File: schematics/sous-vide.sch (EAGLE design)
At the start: 32 parts, among them IC1 MEGA8-P, T1 BC547, T2 BC547, T3 BC547

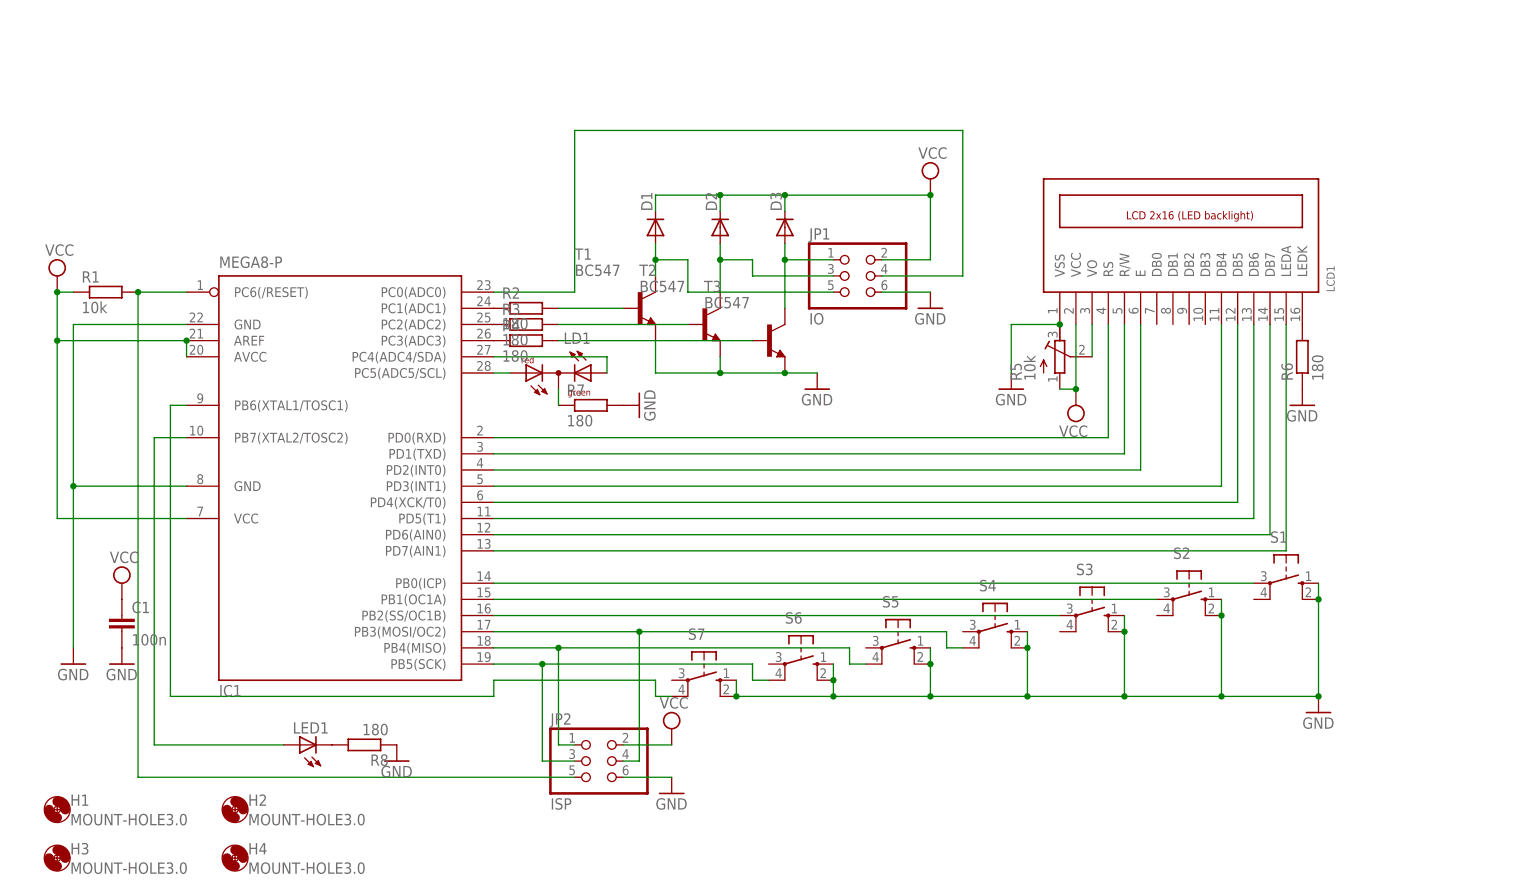
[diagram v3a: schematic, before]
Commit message: Removed button and LED and added crystal for more precise timing over longer periods.
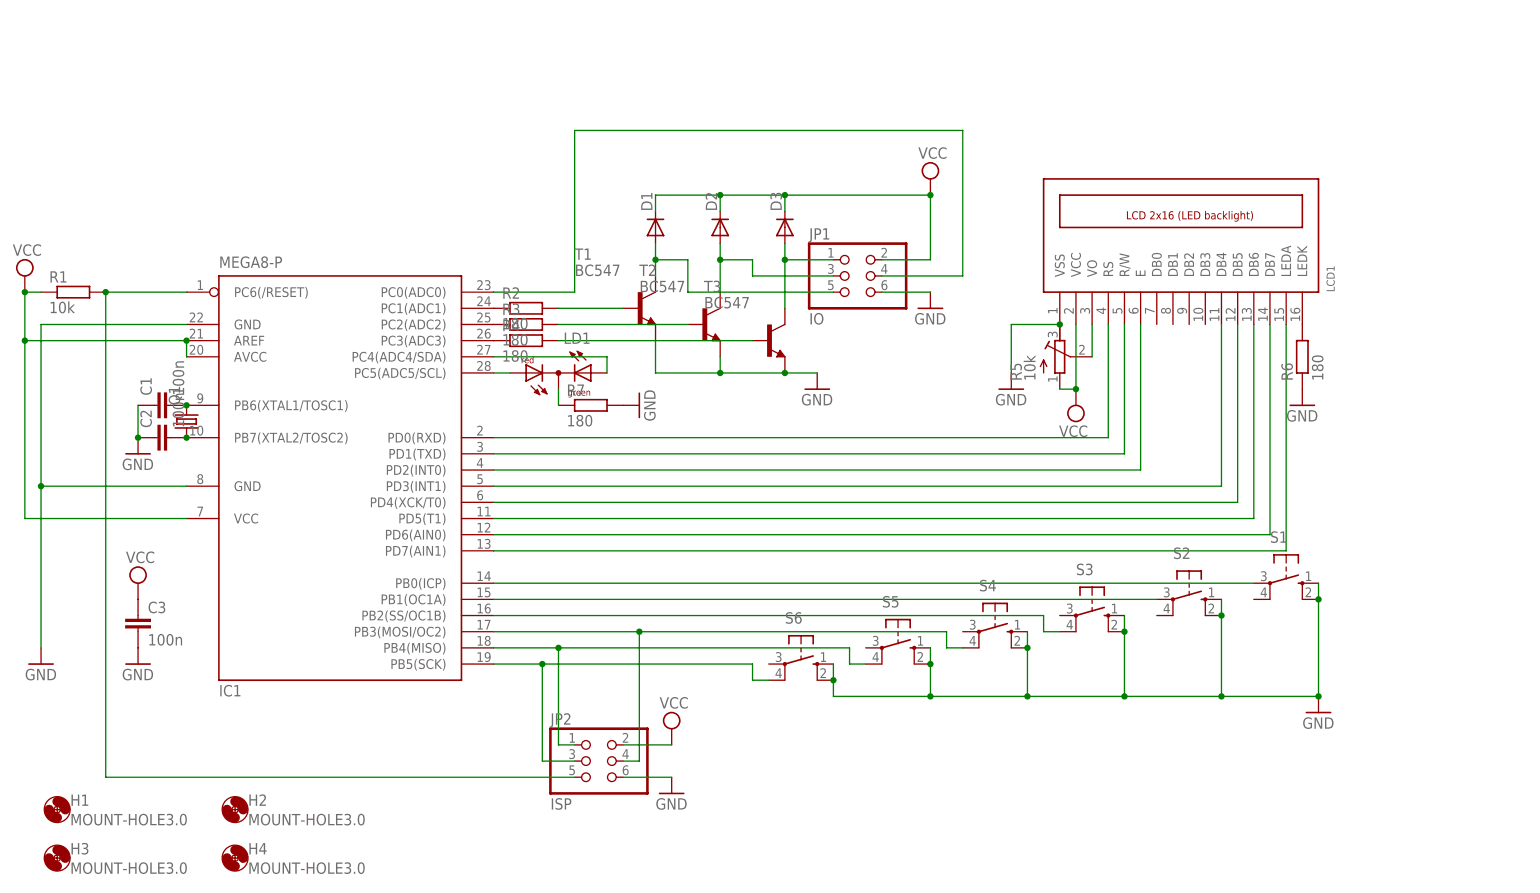
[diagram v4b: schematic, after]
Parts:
- removed LED1: (no value), led:LED3MM
- removed R8: 180, rcl:R-EU_0207/2V
- removed S7: (no value), switch-omron:40-XX
- added C2, C3: 100n, resistor:C-EU025-025X050
- added Q1: (no value), crystal:CRYSTALHC49U-V
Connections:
- removed net N$26: IC1.PB6(XTAL1/TOSC1), S7.P1
- net GND: now also C1.1, C2.1, C3.2; no longer C1.2, R8.1, S7.S, S7.S1
- net N$1: now also C1.2, IC1.PB6(XTAL1/TOSC1), Q1.2; no longer LED1.C, R8.2
- net N$15: now also C2.2, Q1.1; no longer LED1.A
- net N$35: now also S3.P1; no longer S3.P
- net VCC: now also C3.1; no longer C1.1
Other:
- moved on the sheet: C1, R1

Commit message: PCB button and connector layout rearranged. NOT COMPATIBEL WITH PRE-1.5 CODE.
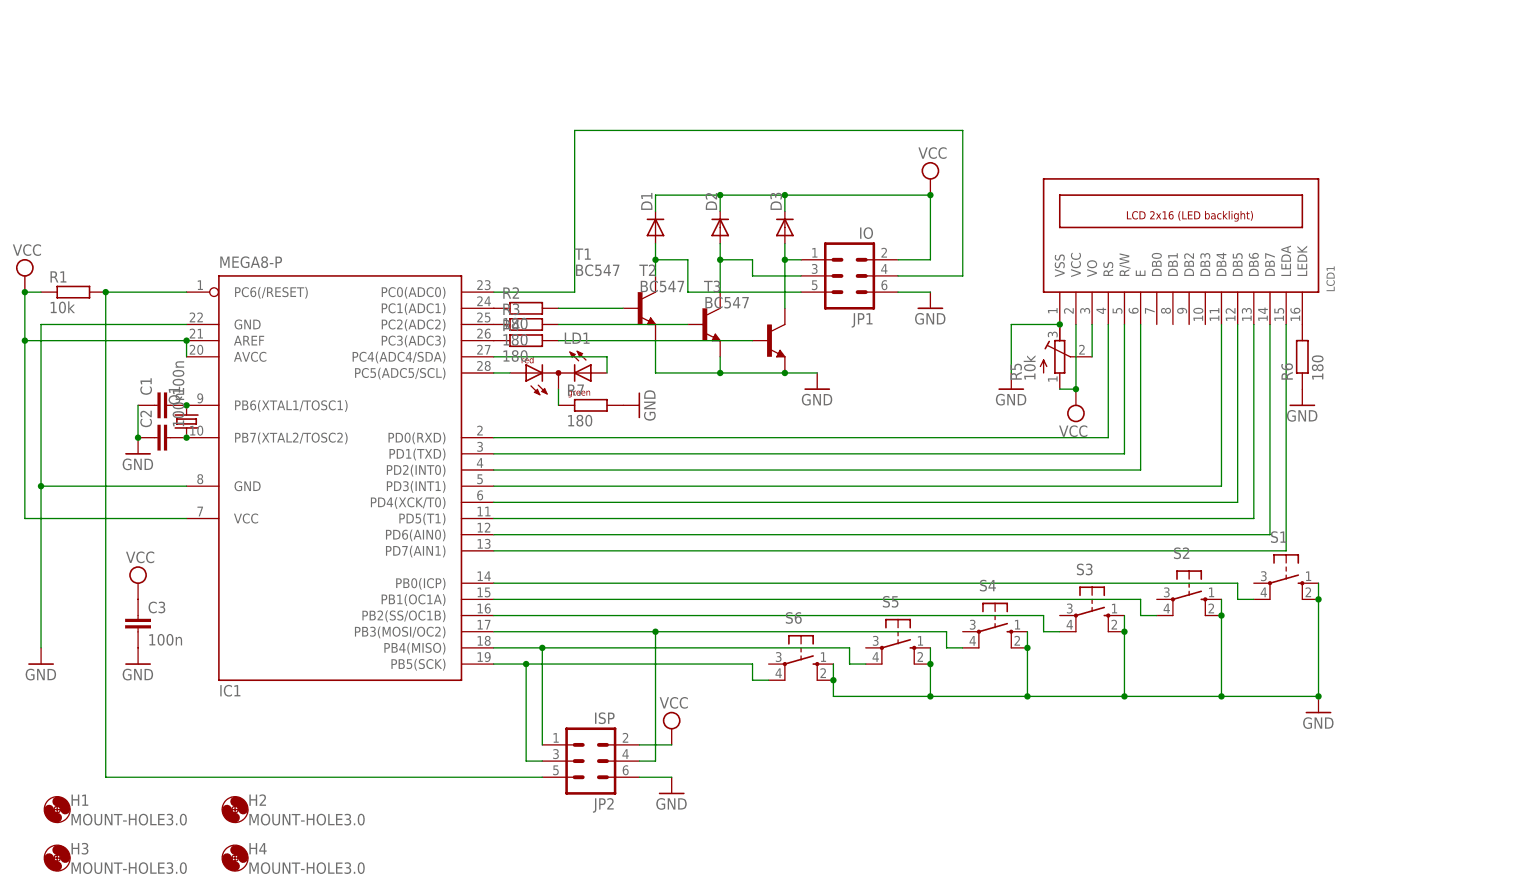
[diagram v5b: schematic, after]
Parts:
- JP1, JP2: device pinhead:PINHD-2X3 -> con-ml:ML6
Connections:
- net N$36: now also S1.P1; no longer S1.P
- net N$37: now also S2.P1; no longer S2.P
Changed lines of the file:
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@@
 <part name="H2" library="holes" deviceset="MOUNT-HOLE" device="3.0"/>
 <part name="H4" library="holes" deviceset="MOUNT-HOLE" device="3.0"/>
-<part name="JP2" library="pinhead" deviceset="PINHD-2X3" device="" value="ISP"/>
+<part name="JP2" library="con-ml" deviceset="ML6" device="" value="ISP"/>
 <part name="SUPPLY5" library="supply2" deviceset="VCC" device=""/>
 <part name="GND10" library="supply1" deviceset="GND" device=""/>
@@
 <part name="R3" library="rcl" deviceset="R-EU_" device="0207/2V" value="180"/>
 <part name="R4" library="rcl" deviceset="R-EU_" device="0207/2V" value="180"/>
-<part name="JP1" library="pinhead" deviceset="PINHD-2X3" device="" value="IO"/>
+<part name="JP1" library="con-ml" deviceset="ML6" device="" value="IO"/>
 <part name="LCD1" library="lcd_2x16_led_backlight" deviceset="LCD_2X16_SIL" device=""/>
 <part name="S6" library="switch-omron" deviceset="40-XX" device=""/>
@@
 <instance part="H2" gate="G$1" x="30.48" y="10.16"/>
 <instance part="H4" gate="G$1" x="30.48" y="2.54"/>
-<instance part="JP2" gate="A" x="86.36" y="17.78"/>
+<instance part="JP2" gate="1" x="86.36" y="17.78" rot="R180"/>
 <instance part="SUPPLY5" gate="G$1" x="99.06" y="22.86"/>
 <instance part="GND10" gate="1" x="99.06" y="12.7"/>
@@
 <instance part="R3" gate="G$1" x="76.2" y="86.36"/>
 <instance part="R4" gate="G$1" x="76.2" y="83.82"/>
-<instance part="JP1" gate="A" x="127" y="93.98"/>
+<instance part="JP1" gate="1" x="127" y="93.98" rot="R180"/>
 <instance part="LCD1" gate="G$1" x="160.02" y="99.06" rot="R90"/>
 <instance part="S6" gate="1" x="119.38" y="33.02" rot="R270"/>
@@
 <net name="GND" class="0">
 <segment>
-<pinref part="JP2" gate="A" pin="6"/>
+<pinref part="JP2" gate="1" pin="6"/>
 <pinref part="GND10" gate="1" pin="GND"/>
-<wire x1="99.06" y1="15.24" x2="91.44" y2="15.24" width="0.1524" layer="91"/>
+<wire x1="99.06" y1="15.24" x2="93.98" y2="15.24" width="0.1524" layer="91"/>
 </segment>
 <segment>
@@
 </segment>
 <segment>
-<pinref part="JP1" gate="A" pin="6"/>
+<pinref part="JP1" gate="1" pin="6"/>
 <pinref part="GND1" gate="1" pin="GND"/>
-<wire x1="139.7" y1="91.44" x2="132.08" y2="91.44" width="0.1524" layer="91"/>
+<wire x1="139.7" y1="91.44" x2="134.62" y2="91.44" width="0.1524" layer="91"/>
 </segment>
 <segment>
@@
 </segment>
 <segment>
-<pinref part="JP2" gate="A" pin="2"/>
+<pinref part="JP2" gate="1" pin="2"/>
 <pinref part="SUPPLY5" gate="G$1" pin="VCC"/>
-<wire x1="99.06" y1="20.32" x2="91.44" y2="20.32" width="0.1524" layer="91"/>
+<wire x1="99.06" y1="20.32" x2="93.98" y2="20.32" width="0.1524" layer="91"/>
 </segment>
 <segment>
@@
 <wire x1="116.84" y1="106.68" x2="139.7" y2="106.68" width="0.1524" layer="91"/>
 <wire x1="139.7" y1="106.68" x2="139.7" y2="96.52" width="0.1524" layer="91"/>
-<pinref part="JP1" gate="A" pin="2"/>
-<wire x1="132.08" y1="96.52" x2="139.7" y2="96.52" width="0.1524" layer="91"/>
+<pinref part="JP1" gate="1" pin="2"/>
+<wire x1="134.62" y1="96.52" x2="139.7" y2="96.52" width="0.1524" layer="91"/>
 <junction x="116.84" y="106.68"/>
 <pinref part="SUPPLY1" gate="G$1" pin="VCC"/>
@@
 <segment>
 <pinref part="IC1" gate="G$1" pin="PB4(MISO)"/>
-<wire x1="81.28" y1="35.56" x2="71.12" y2="35.56" width="0.1524" layer="91"/>
-<pinref part="JP2" gate="A" pin="1"/>
-<wire x1="83.82" y1="20.32" x2="81.28" y2="20.32" width="0.1524" layer="91"/>
-<wire x1="81.28" y1="20.32" x2="81.28" y2="35.56" width="0.1524" layer="91"/>
-<wire x1="81.28" y1="35.56" x2="127" y2="35.56" width="0.1524" layer="91"/>
+<wire x1="78.74" y1="35.56" x2="71.12" y2="35.56" width="0.1524" layer="91"/>
+<pinref part="JP2" gate="1" pin="1"/>
+<wire x1="78.74" y1="20.32" x2="78.74" y2="35.56" width="0.1524" layer="91"/>
+<wire x1="78.74" y1="35.56" x2="127" y2="35.56" width="0.1524" layer="91"/>
 <wire x1="127" y1="35.56" x2="127" y2="33.02" width="0.1524" layer="91"/>
 <pinref part="S5" gate="1" pin="P1"/>
 <wire x1="127" y1="33.02" x2="129.54" y2="33.02" width="0.1524" layer="91"/>
-<junction x="81.28" y="35.56"/>
+<junction x="78.74" y="35.56"/>
 </segment>
 </net>
@@
 <segment>
 <pinref part="IC1" gate="G$1" pin="PB0(ICP)"/>
-<wire x1="71.12" y1="45.72" x2="190.5" y2="45.72" width="0.1524" layer="91"/>
-<pinref part="S1" gate="1" pin="P"/>
+<wire x1="71.12" y1="45.72" x2="187.96" y2="45.72" width="0.1524" layer="91"/>
+<wire x1="187.96" y1="45.72" x2="187.96" y2="43.18" width="0.1524" layer="91"/>
+<pinref part="S1" gate="1" pin="P1"/>
+<wire x1="187.96" y1="43.18" x2="190.5" y2="43.18" width="0.1524" layer="91"/>
 </segment>
 </net>
@@
 <segment>
 <pinref part="IC1" gate="G$1" pin="PB1(OC1A)"/>
-<wire x1="175.26" y1="43.18" x2="71.12" y2="43.18" width="0.1524" layer="91"/>
-<pinref part="S2" gate="1" pin="P"/>
+<wire x1="172.72" y1="43.18" x2="71.12" y2="43.18" width="0.1524" layer="91"/>
+<wire x1="172.72" y1="43.18" x2="172.72" y2="40.64" width="0.1524" layer="91"/>
+<pinref part="S2" gate="1" pin="P1"/>
+<wire x1="172.72" y1="40.64" x2="175.26" y2="40.64" width="0.1524" layer="91"/>
 </segment>
 </net>
 <net name="N$31" class="0">
 <segment>
-<pinref part="JP2" gate="A" pin="5"/>
-<wire x1="10.16" y1="15.24" x2="83.82" y2="15.24" width="0.1524" layer="91"/>
+<pinref part="JP2" gate="1" pin="5"/>
+<wire x1="10.16" y1="15.24" x2="78.74" y2="15.24" width="0.1524" layer="91"/>
 <pinref part="R1" gate="G$1" pin="2"/>
 <wire x1="10.16" y1="15.24" x2="10.16" y2="91.44" width="0.1524" layer="91"/>
@@
 <wire x1="83.82" y1="116.84" x2="144.78" y2="116.84" width="0.1524" layer="91"/>
 <wire x1="144.78" y1="116.84" x2="144.78" y2="93.98" width="0.1524" layer="91"/>
-<pinref part="JP1" gate="A" pin="4"/>
-<wire x1="144.78" y1="93.98" x2="132.08" y2="93.98" width="0.1524" layer="91"/>
+<pinref part="JP1" gate="1" pin="4"/>
+<wire x1="144.78" y1="93.98" x2="134.62" y2="93.98" width="0.1524" layer="91"/>
 </segment>
 </net>
@@
 <segment>
 <pinref part="IC1" gate="G$1" pin="PB3(MOSI/OC2)"/>
-<wire x1="71.12" y1="38.1" x2="93.98" y2="38.1" width="0.1524" layer="91"/>
-<pinref part="JP2" gate="A" pin="4"/>
-<wire x1="91.44" y1="17.78" x2="93.98" y2="17.78" width="0.1524" layer="91"/>
-<wire x1="93.98" y1="17.78" x2="93.98" y2="38.1" width="0.1524" layer="91"/>
-<wire x1="93.98" y1="38.1" x2="142.24" y2="38.1" width="0.1524" layer="91"/>
+<wire x1="71.12" y1="38.1" x2="96.52" y2="38.1" width="0.1524" layer="91"/>
+<pinref part="JP2" gate="1" pin="4"/>
+<wire x1="93.98" y1="17.78" x2="96.52" y2="17.78" width="0.1524" layer="91"/>
+<wire x1="96.52" y1="17.78" x2="96.52" y2="38.1" width="0.1524" layer="91"/>
+<wire x1="96.52" y1="38.1" x2="142.24" y2="38.1" width="0.1524" layer="91"/>
 <wire x1="142.24" y1="38.1" x2="142.24" y2="35.56" width="0.1524" layer="91"/>
 <pinref part="S4" gate="1" pin="P1"/>
 <wire x1="142.24" y1="35.56" x2="144.78" y2="35.56" width="0.1524" layer="91"/>
-<junction x="93.98" y="38.1"/>
+<junction x="96.52" y="38.1"/>
 </segment>
 </net>
@@
 <pinref part="D1" gate="G$1" pin="A"/>
 <wire x1="96.52" y1="93.98" x2="96.52" y2="96.52" width="0.1524" layer="91"/>
-<pinref part="JP1" gate="A" pin="5"/>
+<pinref part="JP1" gate="1" pin="5"/>
 <wire x1="96.52" y1="96.52" x2="96.52" y2="99.06" width="0.1524" layer="91"/>
-<wire x1="124.46" y1="91.44" x2="101.6" y2="91.44" width="0.1524" layer="91"/>
+<wire x1="119.38" y1="91.44" x2="101.6" y2="91.44" width="0.1524" layer="91"/>
 <wire x1="101.6" y1="91.44" x2="101.6" y2="96.52" width="0.1524" layer="91"/>
 <wire x1="101.6" y1="96.52" x2="96.52" y2="96.52" width="0.1524" layer="91"/>
@@
 <pinref part="T2" gate="G$1" pin="C"/>
 <pinref part="D2" gate="G$1" pin="A"/>
-<pinref part="JP1" gate="A" pin="3"/>
+<pinref part="JP1" gate="1" pin="3"/>
 <wire x1="106.68" y1="91.44" x2="106.68" y2="96.52" width="0.1524" layer="91"/>
 <wire x1="106.68" y1="96.52" x2="106.68" y2="99.06" width="0.1524" layer="91"/>
-<wire x1="124.46" y1="93.98" x2="111.76" y2="93.98" width="0.1524" layer="91"/>
+<wire x1="119.38" y1="93.98" x2="111.76" y2="93.98" width="0.1524" layer="91"/>
 <wire x1="106.68" y1="96.52" x2="111.76" y2="96.52" width="0.1524" layer="91"/>
 <wire x1="111.76" y1="96.52" x2="111.76" y2="93.98" width="0.1524" layer="91"/>
@@
 <pinref part="D3" gate="G$1" pin="A"/>
 <wire x1="116.84" y1="88.9" x2="116.84" y2="96.52" width="0.1524" layer="91"/>
-<pinref part="JP1" gate="A" pin="1"/>
+<pinref part="JP1" gate="1" pin="1"/>
 <wire x1="116.84" y1="96.52" x2="116.84" y2="99.06" width="0.1524" layer="91"/>
-<wire x1="124.46" y1="96.52" x2="116.84" y2="96.52" width="0.1524" layer="91"/>
+<wire x1="119.38" y1="96.52" x2="116.84" y2="96.52" width="0.1524" layer="91"/>
 <junction x="116.84" y="96.52"/>
 </segment>
@@
 <segment>
 <pinref part="IC1" gate="G$1" pin="PB5(SCK)"/>
-<wire x1="71.12" y1="33.02" x2="78.74" y2="33.02" width="0.1524" layer="91"/>
-<pinref part="JP2" gate="A" pin="3"/>
-<wire x1="83.82" y1="17.78" x2="78.74" y2="17.78" width="0.1524" layer="91"/>
-<wire x1="78.74" y1="17.78" x2="78.74" y2="33.02" width="0.1524" layer="91"/>
-<wire x1="78.74" y1="33.02" x2="111.76" y2="33.02" width="0.1524" layer="91"/>
+<wire x1="71.12" y1="33.02" x2="76.2" y2="33.02" width="0.1524" layer="91"/>
+<pinref part="JP2" gate="1" pin="3"/>
+<wire x1="78.74" y1="17.78" x2="76.2" y2="17.78" width="0.1524" layer="91"/>
+<wire x1="76.2" y1="17.78" x2="76.2" y2="33.02" width="0.1524" layer="91"/>
+<wire x1="76.2" y1="33.02" x2="111.76" y2="33.02" width="0.1524" layer="91"/>
 <pinref part="S6" gate="1" pin="P1"/>
 <wire x1="114.3" y1="30.48" x2="111.76" y2="30.48" width="0.1524" layer="91"/>
 <wire x1="111.76" y1="33.02" x2="111.76" y2="30.48" width="0.1524" layer="91"/>
-<junction x="78.74" y="33.02"/>
-</segment>
-</net>
+<junction x="76.2" y="33.02"/>
+</segment>
+</net>
